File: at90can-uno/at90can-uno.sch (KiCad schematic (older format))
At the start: 48 parts, among them P1 Power, P2 Analog, P3 Digital, P4 Digital, P5 CONN_01X01, P6 CONN_01X01, P7 CONN_01X01, P8 CONN_01X01

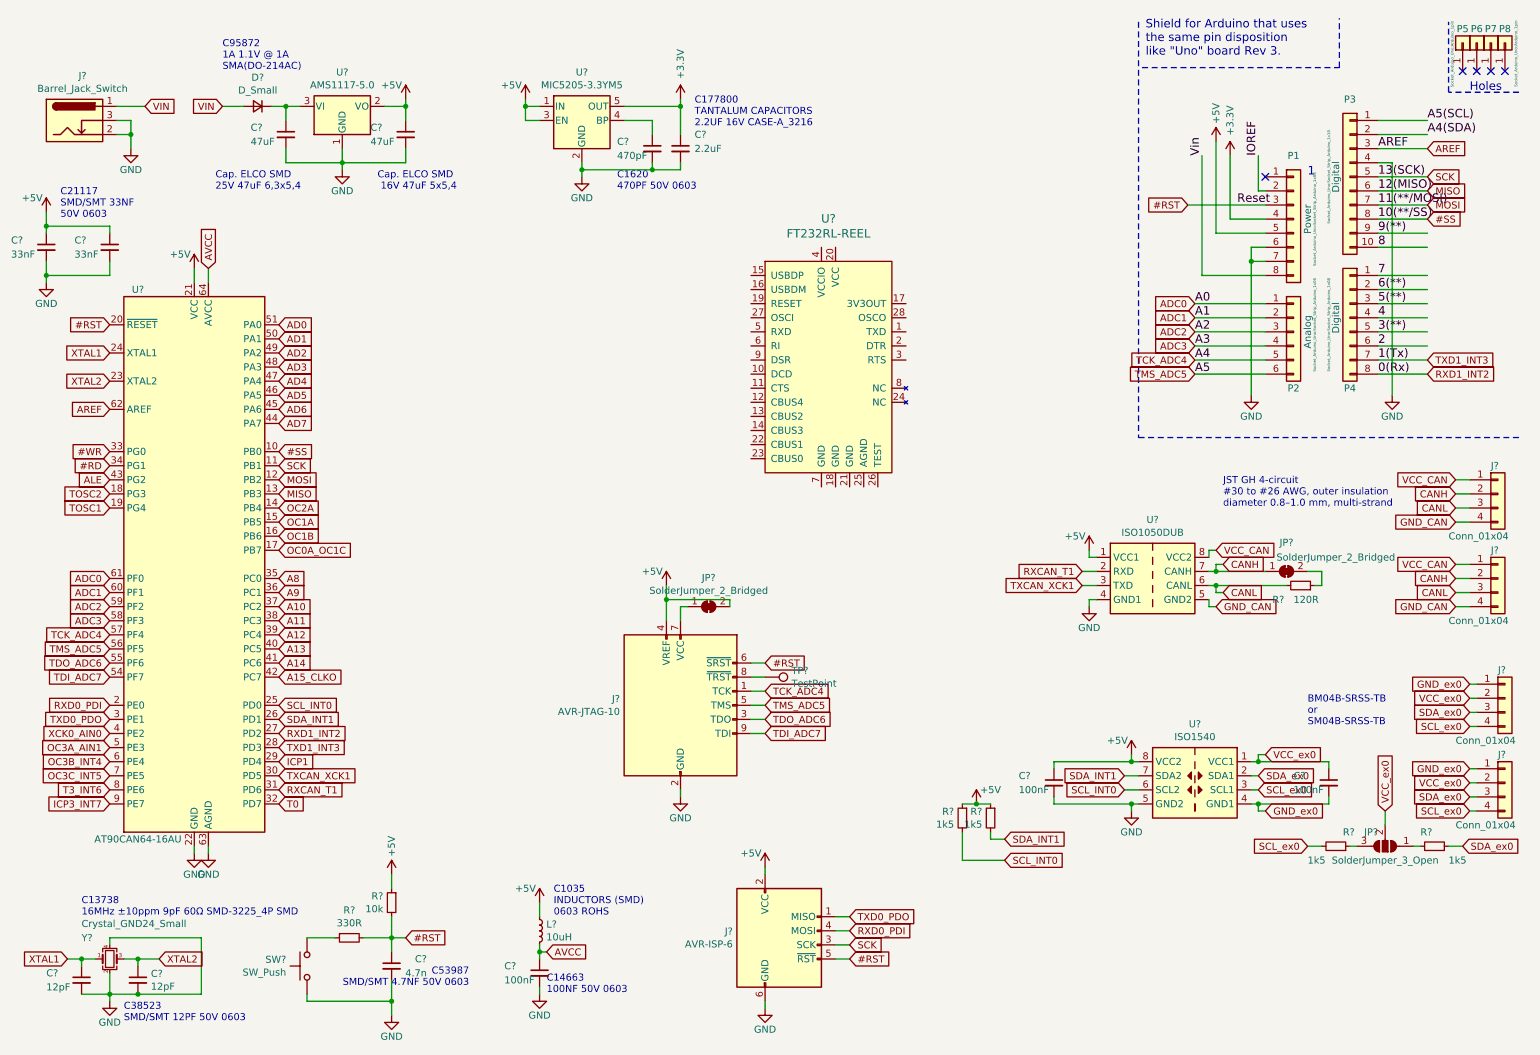
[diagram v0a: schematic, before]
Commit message: update schematic
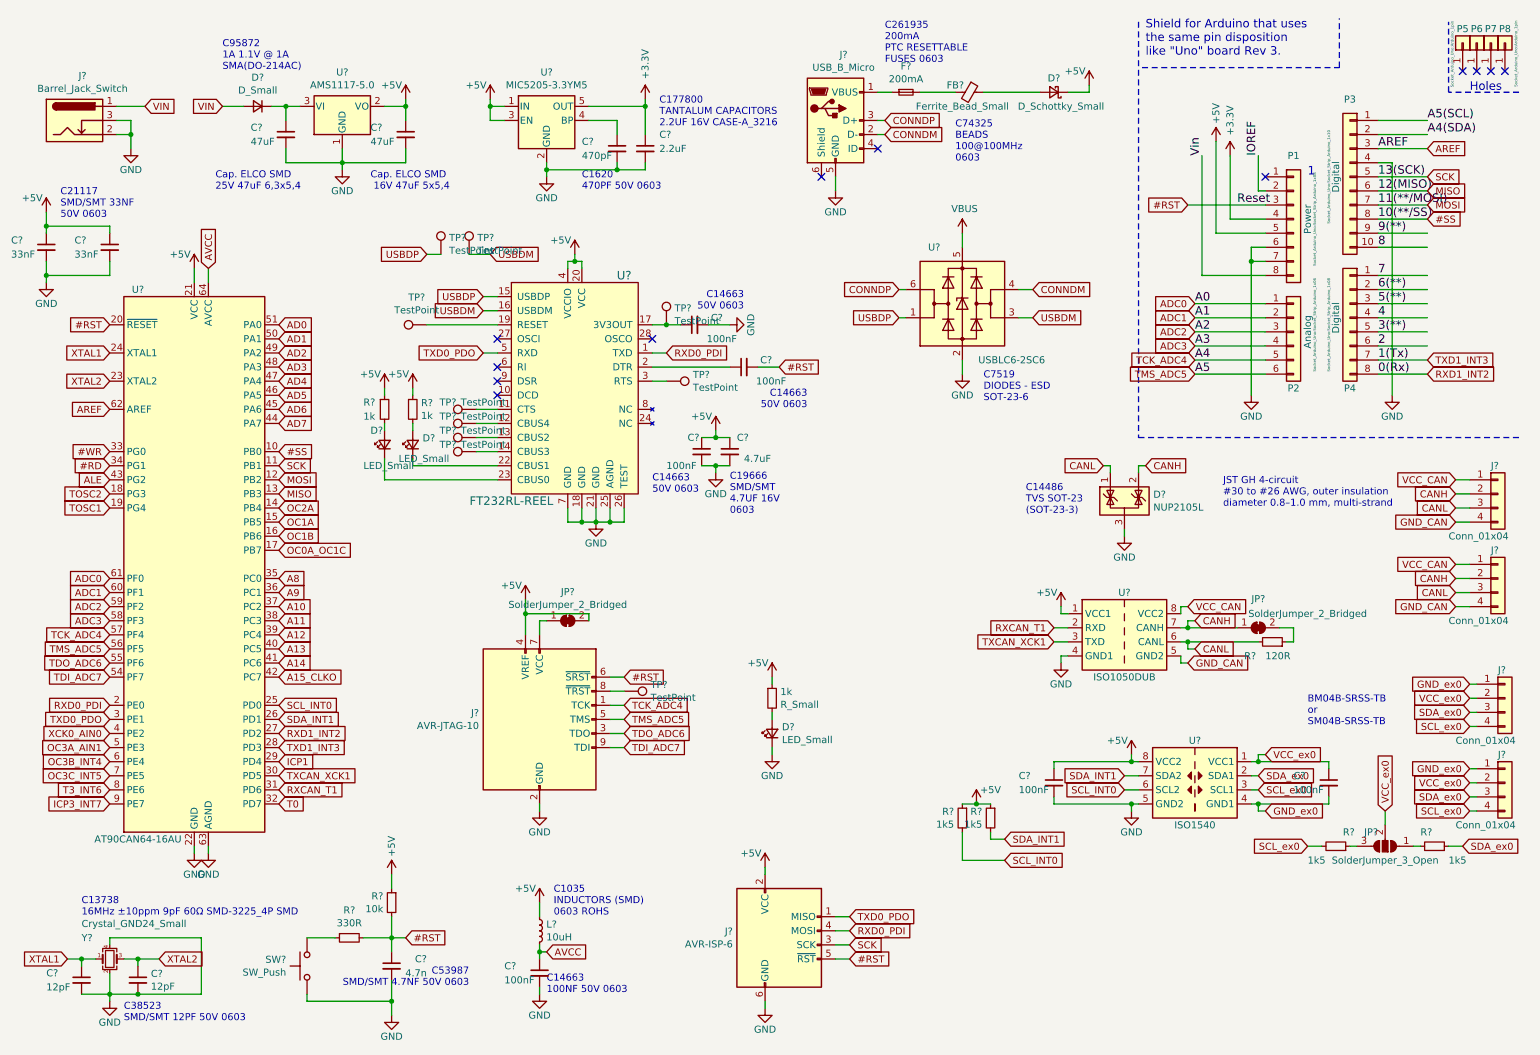
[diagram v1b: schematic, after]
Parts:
- added 1k: R_Small, symbol Device:R_Small
- added C? (x3): 100nF, symbol Device:C_Small
- added C?: 4.7uF, symbol Device:C_Small
- added D?: D_Schottky_Small, symbol Device:D_Schottky_Small
- added D? (x3): LED_Small, symbol Device:LED_Small
- added D?: NUP2105L, Package_TO_SOT_SMD:SOT-23, symbol Power_Protection:NUP2105L
- added F?: 200mA, symbol Device:Fuse_Small
- added FB?: Ferrite_Bead_Small, symbol Device:Ferrite_Bead_Small
- added J?: USB_B_Micro, symbol Connector:USB_B_Micro
- added R? (x2): 1k, symbol Device:R_Small
- added TP? (x9): TestPoint, symbol Connector:TestPoint
- added U?: USBLC6-2SC6, Package_TO_SOT_SMD:SOT-23-6, symbol Power_Protection:USBLC6-2SC6
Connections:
- net labels added: CONNDM, CONNDP, USBDM, USBDP, VBUS
- wire segments 201 -> 268
- no-connect marks 5 -> 12
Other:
- note added: "C14486\nTVS SOT-23\n(SOT-23-3)"
- note added: "C14663\n50V 0603"
- note added: "C19666\nSMD/SMT \n4.7UF 16V \n0603"
- note added: "C261935\n200mA\nPTC RESETTABLE \nFUSES 0603"
- note added: "C74325\nBEADS \n100@100MHz\n0603\n"
- note added: "C7519\nDIODES - ESD \nSOT-23-6"
- moved on the sheet: C?, J?, JP?, R?, TP?, U?

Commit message: update to new kicad
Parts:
- removed D?: D_Small, symbol Device:D_Small
- added D2: D_Schottky_Small, Diode_SMD:D_SOD-123, symbol Device:D_Schottky_Small
- added F2: 500mA, Fuse:Fuse_0603_1608Metric_Pad1.05x0.95mm_HandSolder, symbol Device:Fuse_Small
- added FB2: Ferrite_Bead_Small, Inductor_SMD:L_0603_1608Metric_Pad1.05x0.95mm_HandSolder, symbol Device:Ferrite_Bead_Small
- 1k1: renamed from 1k; footprint (none) -> Resistor_SMD:R_0603_1608Metric_Pad1.05x0.95mm_HandSolder
- C1: renamed from C?; footprint (none) -> Capacitor_SMD:CP_Elec_6.3x5.4
- C10, C11, C12, C13, C14, C15, C16, C3, C5, C6, C7, C8, C9: renamed from C?; footprint (none) -> Capacitor_SMD:C_0603_1608Metric_Pad1.05x0.95mm_HandSolder
- C2: renamed from C?; footprint (none) -> Capacitor_SMD:CP_Elec_5x5.4
- C4: renamed from C?; footprint (none) -> Capacitor_Tantalum_SMD:CP_EIA-3216-18_Kemet-A
- D1: renamed from D?; footprint (none) -> Diode_SMD:D_SOD-123
- D3, D4, D6: renamed from D?; footprint (none) -> LED_SMD:LED_0603_1608Metric_Pad1.05x0.95mm_HandSolder
- F1: renamed from F?; footprint (none) -> Fuse:Fuse_0603_1608Metric_Pad1.05x0.95mm_HandSolder
- FB1: renamed from FB?; footprint (none) -> Inductor_SMD:L_0603_1608Metric_Pad1.05x0.95mm_HandSolder
- J1: renamed from J?; footprint (none) -> Connector_BarrelJack:BarrelJack_CUI_PJ-063AH_Horizontal
- J2: renamed from J?; footprint (none) -> Connector_USB:USB_Micro-B_Amphenol_10103594-0001LF_Horizontal
- J3, J4: renamed from J?; footprint (none) -> Connector_JST:JST_GH_BM04B-GHS-TBT_1x04-1MP_P1.25mm_Vertical
- J5, J7: renamed from J?; footprint (none) -> Connector_JST:JST_SH_BM04B-SRSS-TB_1x04-1MP_P1.00mm_Vertical
- J6: renamed from J?; footprint (none) -> Connector_IDC:IDC-Header_2x05_P2.54mm_Vertical
- J8: renamed from J?; footprint (none) -> Connector_IDC:IDC-Header_2x03_P2.54mm_Vertical
- JP1, JP2: renamed from JP?; footprint (none) -> Jumper:SolderJumper-2_P1.3mm_Bridged_Pad1.0x1.5mm
- JP3: renamed from JP?; footprint (none) -> Jumper:SolderJumper-3_P1.3mm_Open_Pad1.0x1.5mm_NumberLabels
- L1: renamed from L?; footprint (none) -> Inductor_SMD:L_0603_1608Metric_Pad1.05x0.95mm_HandSolder
- R1, R2, R3, R4, R5, R6, R7, R8, R9: renamed from R?; footprint (none) -> Resistor_SMD:R_0603_1608Metric_Pad1.05x0.95mm_HandSolder
- SW1: renamed from SW?; footprint (none) -> Switches:TACTILE_SWITCH_SMD_6.0X3.5MM
- TP1, TP10, TP2, TP3, TP4, TP5, TP6, TP7, TP8, TP9: renamed from TP?; footprint (none) -> Connector_Pin:Pin_D0.7mm_L6.5mm_W1.8mm_FlatFork
- Y1: renamed from Y?; footprint (none) -> Crystal:Crystal_SMD_3225-4Pin_3.2x2.5mm_HandSoldering
- gave numbers to parts that had none: 8
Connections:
- net 2 is gone; now on net T3_INT6: P4.6 (Pin_6)
- net 3(**) is gone; now on net OC3C_INT5: P4.5 (Pin_5)
- net 4 is gone; now on net OC2A: P4.4 (Pin_4)
- net 5(**) is gone; now on net OC3B_INT4: P4.3 (Pin_3)
- net 6(**) is gone; now on net OC3A_AIN1: P4.2 (Pin_2)
- net 7 is gone; now on net XCK0_AIN0: P4.1 (Pin_1)
- net 8 is gone; now on net OC1A: P3.10 (Pin_10)
- net 9(**) is gone; now on net OC1B: P3.9 (Pin_9)
- net A4(SDA) is gone; now on net SDA_INT1: P3.2 (Pin_2)
- net A5(SCL) is gone; now on net SCL_INT0: P3.1 (Pin_1)
- net Vin is gone; now on net VIN: P1.8 (Pin_8)
- net VBUS: now also D1.2 (A), FB1.1
- net VIN: now also F2.1
- net at C1.1, U1.3 (VI): now also D2.1 (K)
- new net: F2.2, FB2.2
- new net: D2.2 (A), FB2.1
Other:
- note added: "C261937\nTLC-FSMD050\nPTC RESETTABLE \n500mA FUSES \n0603"
- note added: "C8598\nB5819W\nSCHOTTKY BARRIER \nDIODES SOD-123"
- note removed: "C95872\n1A 1.1V @ 1A \nSMA(DO-214AC)"
